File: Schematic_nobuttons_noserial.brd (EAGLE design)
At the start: 100.2 x 85.8 mm, 19 parts, among them X1 1503_02

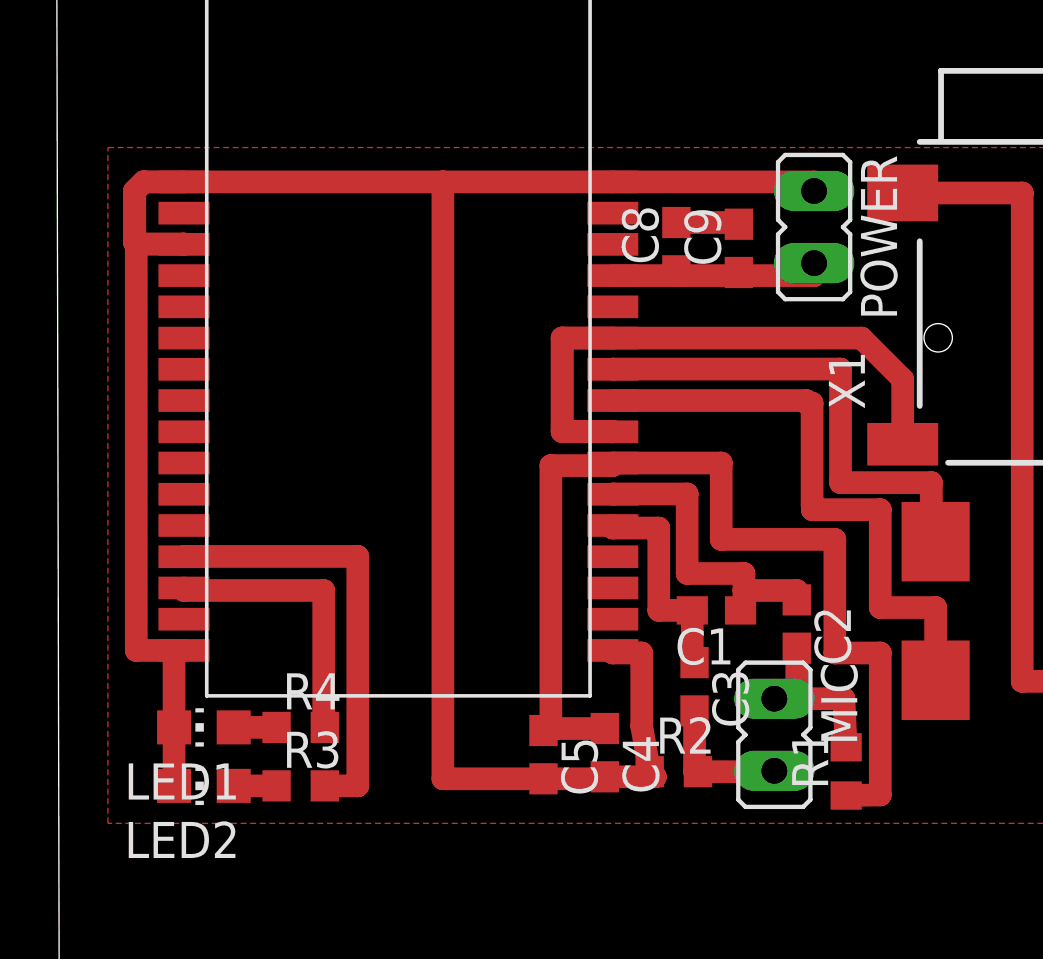
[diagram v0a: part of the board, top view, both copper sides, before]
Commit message: updated library pads position to go a bit under the module so they can be soldered easier
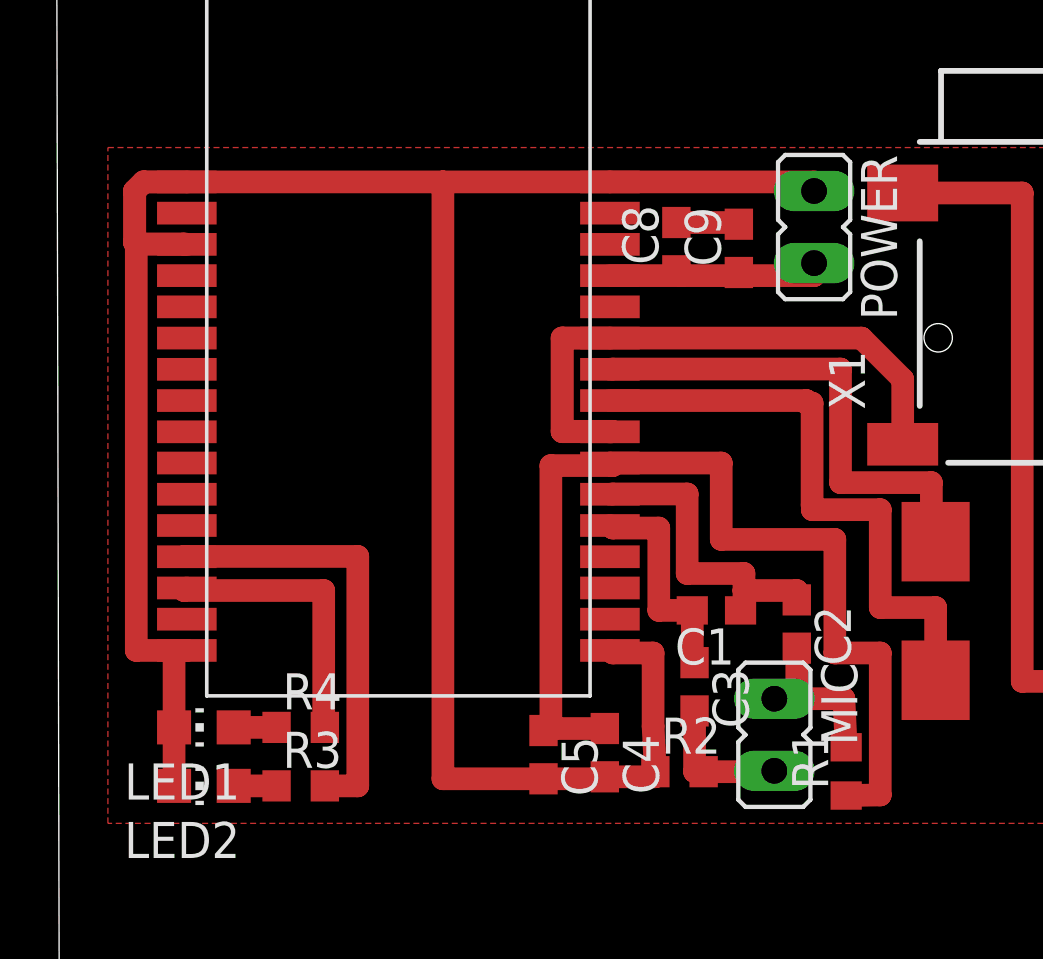
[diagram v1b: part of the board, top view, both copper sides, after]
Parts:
- moved R2 0.20 mm to (21.7, 57.0)
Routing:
- net GND: track 85.5 -> 86.1 mm
